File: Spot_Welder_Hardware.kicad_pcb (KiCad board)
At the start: 2 copper layers, 147 parts, among them J1 Mini USB, J2 Conn_01x03_Male, Q1 Q_NMOS_GSD, Q10 Q_NMOS_GDS, Q11 Q_NMOS_GDS, Q12 Q_NMOS_GDS, Q13 Q_NMOS_GDS, Q2 2N2219, Q3 Q_NMOS_GDS, Q4 Q_NMOS_GDS, Q5 Q_NMOS_GDS, Q6 Q_NMOS_GDS, Q7 Q_NMOS_GDS, Q8 Q_NMOS_GDS, Q9 Q_NMOS_GDS, SW1 SW_Push, SW2 SW_SPDT, SW3 Lead Voltage Trigger, SW4 SW_Push, U1 OKI, U2 ATMEGA328P, U3 FAN3122TMXCT-ND, U4 FT232RL, U5 FAN3122TMXCT-ND, Y1 Crystal

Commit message: Started board layout
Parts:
- moved D10 581.1 mm to (-103.8, 214.6)
- moved R20 560.5 mm to (-113.7, 199.4)
- moved R18 556.0 mm to (-105.2, 190.5)
- moved R23 502.9 mm to (-39.2, 41.9)
- moved R36 500.8 mm to (-39.2, 55.2)
- moved R19 500.3 mm to (-98.3, 201.3)
- moved Conn2 492.8 mm to (-68.6, 156.2)
- moved L2 481.3 mm to (-32.9, 42.5)
- moved R26 475.0 mm to (-39.2, 43.8)
- moved L7 469.8 mm to (-32.9, 52.1)
- moved R30 469.4 mm to (-39.2, 49.5)
- moved R28 466.3 mm to (-39.2, 45.7)
- moved R38 451.0 mm to (-39.2, 57.1)
- moved L4 442.6 mm to (-32.9, 46.4)
- moved Q2 438.4 mm to (-117.5, 189.2)
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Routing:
- net Net-(R13-Pad1): track 0.00 -> 7.62 mm
- net Net-(R12-Pad1): track 0.00 -> 7.62 mm
- net Net-(R25-Pad2): track 0.00 -> 3.17 mm
- net Net-(R24-Pad2): track 0.00 -> 3.17 mm
- added copper zone on F.Cu, net GND
- added copper zone on B.Cu, net V+

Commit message: High-lvel power placemet
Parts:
- D12, R21: moved to B.Cu
- moved Q3 434.1 mm to (-65.8, 23.7)
- moved SW2 426.9 mm to (-84.2, 22.9), turned to 90 degrees
- moved SW4 400.0 mm to (19.1, 139.1)
- moved D12 381.6 mm to (-40.6, 3.81)
- moved R21 365.3 mm to (-40.5, 6.99)
- moved C43 353.9 mm to (-39.1, 30.2), turned to 270 degrees
- moved U1 337.5 mm to (-41.0, 27.3), turned to 270 degrees
- moved C44 321.9 mm to (-39.1, 34.6), turned to 270 degrees
- moved R14 268.8 mm to (-58.4, 0.00), turned to 180 degrees
- moved R12 262.1 mm to (-58.4, 15.2), turned to 180 degrees
- moved C32 255.9 mm to (56.5, 59.1), turned to 90 degrees
- moved C23 240.8 mm to (60.3, 59.1), turned to 180 degrees
- moved C24 237.1 mm to (60.3, 71.8), turned to 180 degrees
- moved R13 224.6 mm to (-88.9, 7.62), turned to 0 degrees
- moved C15 214.0 mm to (92.7, 34.9), turned to 90 degrees
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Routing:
- net Net-(R23-Pad2): track 0.00 -> 185.0 mm
- net Net-(R31-Pad2): track 0.00 -> 122.6 mm
- net VIN: track 0.00 -> 22.6 mm
- net Net-(Q2-Pad3): track 0.00 -> 16.8 mm
- net VS: track 0.00 -> 10.4 mm
- net Net-(Q2-Pad2): track 0.00 -> 10.4 mm
- net Net-(L6-Pad1): track 0.00 -> 8.11 mm
- net Net-(L5-Pad1): track 0.00 -> 7.22 mm
- net GND: track 0.00 -> 6.02 mm
- net Pulse_Out: track 0.00 -> 5.71 mm
- net Net-(L9-Pad1): track 0.00 -> 4.79 mm
- net Net-(L8-Pad1): track 0.00 -> 4.79 mm
- net Net-(L10-Pad1): track 0.00 -> 4.79 mm
- net Net-(L3-Pad1): track 0.00 -> 4.71 mm
- net Net-(L2-Pad1): track 0.00 -> 4.71 mm
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- added copper zone on B.Cu, net GND
- added copper zone on F.Cu, net V+
- removed copper zone on F.Cu, net GND
- removed copper zone on B.Cu, net V+

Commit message: Placed components and routed all signal
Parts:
- Conn3: value Anderson_2 -> AndersonPP
- moved J1 611.4 mm to (-50.2, 78.9), turned to 90 degrees
- moved D17 591.9 mm to (-36.8, 81.7)
- moved R35 591.9 mm to (-36.8, 77.0)
- moved D18 591.3 mm to (-34.3, 81.7)
- moved R37 591.3 mm to (-34.3, 77.0)
- moved D20 590.7 mm to (-31.8, 81.7)
- moved R39 590.7 mm to (-31.8, 77.0)
- moved C46 589.5 mm to (-48.2, 68.5), turned to 270 degrees
- moved C47 583.3 mm to (-45.8, 68.5), turned to 90 degrees
- moved U4 580.7 mm to (-45.2, 59.7), turned to 270 degrees
- moved C48 568.5 mm to (-39.7, 53.3), turned to 0 degrees
- moved J2 552.9 mm to (-41.9, 81.3), turned to 180 degrees
- moved SW1 550.8 mm to (-76.2, 73.7), turned to 180 degrees
- moved D8 548.4 mm to (18.7, 33.0), turned to 180 degrees
- moved R10 546.2 mm to (24.0, 33.0), turned to 0 degrees
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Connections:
- C43 pad 1: VIN -> /Vin
- C45 pad 1: VIN -> /Vin
- Conn3 pad 1: V+ -> Conn_GND
- Conn3 pad 2: Conn_GND -> V+
- D12 pad 1: VIN -> /Vin
- R21 pad 1: VIN -> /Vin
- U1 pad 1: VIN -> /Vin
- U2 pad 14: 5V_Ind -> (no net)
- U2 pad 15: 7.5V_Ind -> 12.5V_Ind
- U2 pad 17: 12.5V_Ind -> 7.5V_Ind
- U2 pad 18: (no net) -> 5V_Ind
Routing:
- net Reset: track 0.00 -> 110.1 mm
- net Pulse_Out: track 5.71 -> 113.0 mm, vias 0 -> 2
- net IC_TX: track 0.00 -> 83.8 mm, vias 0 -> 1
- net IC_RX: track 0.00 -> 79.4 mm, vias 0 -> 1
- net USB+5V: track 0.00 -> 59.5 mm, vias 0 -> 2
- net Buzzer: track 0.00 -> 29.9 mm
- net Net-(D18-Pad1): track 0.00 -> 27.6 mm
- net Net-(D17-Pad1): track 0.00 -> 26.6 mm
- net DTR: track 0.00 -> 26.3 mm, vias 0 -> 1
- net 5V_Ind: track 0.00 -> 23.7 mm
- net Lead_Sense: track 0.00 -> 23.1 mm
- net V_Sense: track 0.00 -> 21.6 mm
- net Ext_Trigger: track 0.00 -> 19.1 mm
- net 7.5V_Ind: track 0.00 -> 19.0 mm
- net D-: track 0.00 -> 17.7 mm
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
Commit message: Moved around Components
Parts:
- moved R3 1.61 mm to (-7.62, 76.0)
- moved R6 1.61 mm to (-5.08, 76.0)
- moved R8 1.61 mm to (-10.2, 76.0)
- moved D2 1.27 mm to (-7.62, 81.1)
- moved D4 1.27 mm to (-5.08, 81.1)
- moved D6 1.27 mm to (-10.2, 81.1)
- moved R35 0.97 mm to (-36.8, 76.0)
- moved R37 0.97 mm to (-34.3, 76.0)
- moved R39 0.97 mm to (-31.8, 76.0)
- moved D17 0.64 mm to (-36.8, 81.1)
- moved D18 0.64 mm to (-34.3, 81.1)
- moved D20 0.64 mm to (-31.8, 81.1)
- moved R1 0.59 mm to (22.9, 76.0)
- moved R5 0.59 mm to (20.3, 76.0)
- moved R7 0.59 mm to (17.8, 76.0)
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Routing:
- net USB+5V: track 59.5 -> 51.5 mm
- net Ext_Trigger: track 19.1 -> 17.7 mm
- net 7.5V_Ind: track 19.0 -> 18.5 mm
- net 5V_Ind: track 23.7 -> 23.1 mm
- net 12.5V_Ind: track 8.96 -> 8.37 mm
- net 10V_Ind: track 14.0 -> 13.4 mm
- net Net-(D17-Pad1): track 26.6 -> 26.0 mm
- removed copper zone on B.Cu, net GND
- removed copper zone on F.Cu, net V+

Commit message: Created Polygons
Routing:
- added copper zone on F.Cu, net +5V
- added copper zone on F.Cu, net /Vin
- added copper zone on B.Cu, net GND
- added copper zone on B.Cu, net Power_GND
- added copper zone on F.Cu, net V+
- added copper zone on F.Cu, net VS
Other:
- board outline added: 256.5 x 182.9 mm
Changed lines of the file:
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@@
   (general
     (thickness 1.6)
-    (drawings 3)
+    (drawings 10)
     (tracks 349)
     (zones 0)
@@
   )
   (setup
-    (last_trace_width 0.381)
+    (last_trace_width 0.25)
     (user_trace_width 0.254)
     (user_trace_width 0.381)
@@
     )
   )
-  (gr_line (start 53.975 83.82) (end -92.075 83.82) (layer Edge.Cuts) (width 0.15))
+  (gr_line (start 160.02 83.82) (end -86.36 83.82) (layer Edge.Cuts) (width 0.15))
+  (gr_line (start 165.1 78.74) (end 165.1 -93.98) (layer Edge.Cuts) (width 0.15))
+  (gr_line (start 160.02 -99.06) (end -86.36 -99.06) (layer Edge.Cuts) (width 0.15))
+  (gr_arc (start 160.02 -93.98) (end 165.1 -93.98) (angle -90) (layer Edge.Cuts) (width 0.15))
+  (gr_arc (start 160.02 78.74) (end 160.02 83.82) (angle -90) (layer Edge.Cuts) (width 0.15))
+  (gr_arc (start -86.36 78.74) (end -91.44 78.74) (angle -90) (layer Edge.Cuts) (width 0.15))
+  (gr_arc (start -86.36 -93.98) (end -86.36 -99.06) (angle -90) (layer Edge.Cuts) (width 0.15))
+  (gr_line (start -91.44 78.74) (end -91.44 -93.98) (layer Edge.Cuts) (width 0.15))
   (gr_line (start -91.44 254) (end -91.44 -254) (layer F.SilkS) (width 0.2))
   (gr_line (start -254 84.836) (end 254 84.836) (layer F.SilkS) (width 0.2))
@@
   (segment (start -39.751 29.845) (end -39.116 29.21) (width 0.381) (layer F.Cu) (net 74))
   (segment (start -42.291 29.845) (end -39.751 29.845) (width 0.381) (layer F.Cu) (net 74))
+  (zone (net 27) (net_name VS) (layer F.Cu) (hatch edge 0.508)
+    (connect_pads yes (clearance 0.508))
+    (min_thickness 0.254)
+    (fill yes (arc_segments 16) (thermal_gap 0.508) (thermal_bridge_width 0.508))
+    (polygon
+      (pts
+        (xy 68.58 83.82) (xy 68.58 42.545) (xy 113.03 42.545) (xy 113.03 83.82)
+      )
+    )
+  )
+  (zone (net 3) (net_name V+) (layer F.Cu) (hatch edge 0.508)
+    (connect_pads (clearance 0.508))
+    (min_thickness 0.254)
+    (fill yes (arc_segments 16) (thermal_gap 0.508) (thermal_bridge_width 0.508))
+    (polygon
+      (pts
+        (xy 113.538 83.82) (xy 113.538 42.164) (xy 68.072 42.164) (xy 68.072 83.82) (xy 57.404 83.82)
+        (xy 57.404 26.416) (xy -23.876 26.416) (xy -23.876 -4.064) (xy -56.134 -4.064) (xy -56.134 69.596)
+        (xy -91.44 69.596) (xy -91.44 -99.06) (xy 165.1 -99.06) (xy 165.1 83.82)
+      )
+    )
+  )
+  (zone (net 1) (net_name +5V) (layer F.Cu) (hatch edge 0.508)
+    (connect_pads yes (clearance 0.508))
+    (min_thickness 0.254)
+    (fill yes (arc_segments 16) (thermal_gap 0.508) (thermal_bridge_width 0.508))
+    (polygon
+      (pts
+        (xy 56.896 83.82) (xy 56.896 26.924) (xy -23.876 26.924) (xy -23.876 32.766) (xy -55.626 33.02)
+        (xy -55.626 70.104) (xy -91.44 70.104) (xy -91.44 83.82) (xy 46.99 83.82)
+      )
+    )
+  )
+  (zone (net 74) (net_name /Vin) (layer F.Cu) (hatch edge 0.508)
+    (connect_pads (clearance 0.508))
+    (min_thickness 0.254)
+    (fill yes (arc_segments 16) (thermal_gap 0.508) (thermal_bridge_width 0.508))
+    (polygon
+      (pts
+        (xy -24.384 32.258) (xy -55.626 32.512) (xy -55.626 -3.556) (xy -24.384 -3.556)
+      )
+    )
+  )
+  (zone (net 4) (net_name GND) (layer B.Cu) (hatch edge 0.508)
+    (connect_pads yes (clearance 0.508))
+    (min_thickness 0.254)
+    (fill yes (arc_segments 16) (thermal_gap 0.508) (thermal_bridge_width 0.508))
+    (polygon
+      (pts
+        (xy 165.1 83.82) (xy 165.1 -99.06) (xy -91.44 -99.06) (xy -91.44 19.558) (xy -57.404 19.558)
+        (xy -57.404 69.85) (xy -91.44 69.85) (xy -91.44 83.82)
+      )
+    )
+  )
+  (zone (net 25) (net_name Power_GND) (layer B.Cu) (hatch edge 0.508)
+    (connect_pads yes (clearance 0.508))
+    (min_thickness 0.254)
+    (fill yes (arc_segments 16) (thermal_gap 0.508) (thermal_bridge_width 0.508))
+    (polygon
+      (pts
+        (xy -91.44 69.342) (xy -57.912 69.342) (xy -57.912 20.066) (xy -91.44 20.066)
+      )
+    )
+  )
 )

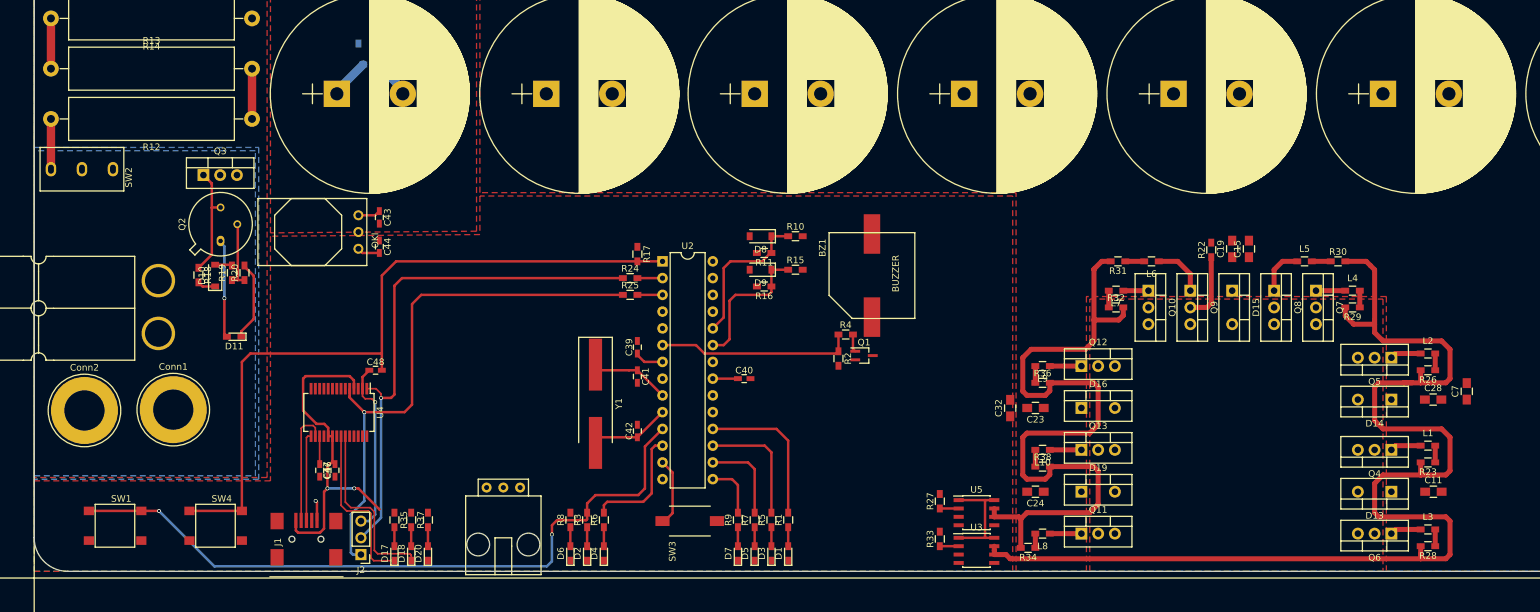
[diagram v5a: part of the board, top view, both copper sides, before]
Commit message: Finished Fill Zones and grounding
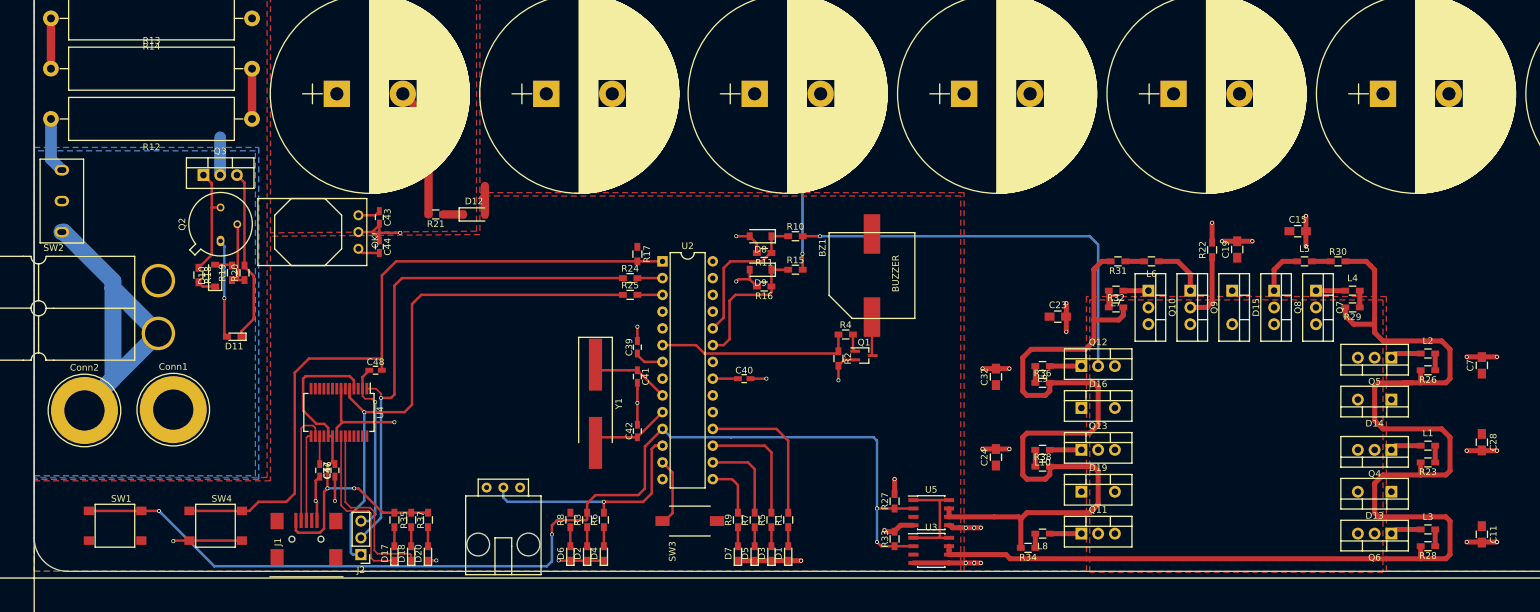
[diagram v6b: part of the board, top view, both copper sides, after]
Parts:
- D12, R21: moved to F.Cu
- moved D12 30.4 mm to (-24.8, 29.7)
- moved R21 24.8 mm to (-30.6, 29.7), turned to 180 degrees
- moved C23 14.3 mm to (63.7, 45.2), turned to 0 degrees
- moved C28 9.81 mm to (128.0, 64.2), turned to 270 degrees
- moved C11 9.78 mm to (128.0, 78.2), turned to 270 degrees
- moved C24 7.95 mm to (54.4, 66.5), turned to 90 degrees
- moved C15 7.86 mm to (100.1, 32.3), turned to 0 degrees
- moved R27 6.86 mm to (39.0, 73.2)
- moved R33 6.86 mm to (39.0, 78.9)
- moved U3 6.86 mm to (44.5, 80.6)
- moved U5 6.86 mm to (44.5, 74.9)
- moved SW2 5.71 mm to (-87.2, 27.7), turned to 0 degrees
- moved C32 5.21 mm to (54.4, 54.3)
- moved C7 4.55 mm to (128.0, 52.6)
- moved C19 0.77 mm to (90.9, 35.0)
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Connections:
- SW3 pad 1: V+ -> +5V
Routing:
- net GND: track 9.05 -> 178.6 mm, vias 1 -> 39
- net VS: track 10.4 -> 74.2 mm, vias 0 -> 1
- net Pulse_Out: track 113.1 -> 167.3 mm, vias 2 -> 4
- net Conn_GND: track 0.00 -> 52.8 mm
- net V+: track 2.80 -> 20.2 mm, vias 0 -> 2
- net Ext_Trigger: track 17.7 -> 35.0 mm, vias 0 -> 1
- net Power_GND: track 12.1 -> 26.3 mm
- net USB+5V: track 51.5 -> 59.0 mm
- net Net-(R23-Pad2): track 183.8 -> 190.7 mm
- net Net-(R31-Pad2): track 114.9 -> 121.7 mm
- net Net-(BZ1-Pad2): track 0.00 -> 5.88 mm
- net Reset: track 110.1 -> 107.2 mm
- net /Vin: track 9.54 -> 6.94 mm
- net Net-(R12-Pad2): track 7.62 -> 8.43 mm

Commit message: Added 6-32 Mounting Holes
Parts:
- added REF**: 6-32 Screw Hole, Project Library:6-32 Screw Hole, F.Cu at (-98.8, 78.0)
- added REF**: 6-32 Screw Hole, Project Library:6-32 Screw Hole, F.Cu at (-87.6, 78.7)
- added REF**: 6-32 Screw Hole, Project Library:6-32 Screw Hole, F.Cu at (162.6, -96.5)
- added REF**: 6-32 Screw Hole, Project Library:6-32 Screw Hole, F.Cu at (-88.9, -96.5)
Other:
- outline, holes or cut-outs redrawn
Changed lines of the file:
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@@
   (general
     (thickness 1.6)
-    (drawings 10)
+    (drawings 14)
     (tracks 525)
     (zones 0)
-    (modules 147)
+    (modules 151)
     (nets 75)
   )
@@
   )
   (setup
-    (last_trace_width 1.27)
+    (last_trace_width 0.25)
     (user_trace_width 0.254)
     (user_trace_width 0.381)
@@
     (mod_text_size 1 1)
     (mod_text_width 0.15)
-    (pad_size 1.524 1.524)
+    (pad_size 3.683 3.683)
     (pad_drill 0.762)
     (pad_to_mask_clearance 0.2)
@@
     (add_net V_Sense)
   )
+  (module "Project Library:6-32 Screw Hole" (layer F.Cu)
+    (at -98.806 77.978)
+    (fp_text reference REF** (at 0 0.5) (layer F.SilkS) hide
+      (effects (font (size 1 1) (thickness 0.15)))
+    )
+    (fp_text value "6-32 Screw Hole" (at 0 -0.5) (layer F.Fab)
+      (effects (font (size 1 1) (thickness 0.15)))
+    )
+    (pad "" np_thru_hole circle (at 261.366 0.762) (size 3.683 3.683) (drill 0.762) (layers *.Cu *.Mask))
+  )
+  (module "Project Library:6-32 Screw Hole" (layer F.Cu)
+    (at -87.63 78.74)
+    (fp_text reference REF** (at 0 0.5) (layer F.SilkS) hide
+      (effects (font (size 1 1) (thickness 0.15)))
+    )
+    (fp_text value "6-32 Screw Hole" (at 0 -0.5) (layer F.Fab)
+      (effects (font (size 1 1) (thickness 0.15)))
+    )
+    (pad "" np_thru_hole circle (at -1.27 0) (size 3.683 3.683) (drill 0.762) (layers *.Cu *.Mask))
+  )
+  (module "Project Library:6-32 Screw Hole" (layer F.Cu)
+    (at 162.56 -96.52)
+    (fp_text reference REF** (at 0 0.5) (layer F.SilkS) hide
+      (effects (font (size 1 1) (thickness 0.15)))
+    )
+    (fp_text value "6-32 Screw Hole" (at 0 -0.5) (layer F.Fab)
+      (effects (font (size 1 1) (thickness 0.15)))
+    )
+    (pad "" np_thru_hole circle (at 0 0) (size 3.683 3.683) (drill 0.762) (layers *.Cu *.Mask))
+  )
   (module MRDT_Devices:BUZZER_SMI_1324_TW_5V_2_R (layer F.Cu)
     (at 35.56 32.48 270)
@@
     )
   )
+  (module "Project Library:6-32 Screw Hole" (layer F.Cu)
+    (at -88.9 -96.52)
+    (fp_text reference REF** (at 0 0.5) (layer F.SilkS) hide
+      (effects (font (size 1 1) (thickness 0.15)))
+    )
+    (fp_text value "6-32 Screw Hole" (at 0 -0.5) (layer F.Fab)
+      (effects (font (size 1 1) (thickness 0.15)))
+    )
+    (pad "" np_thru_hole circle (at 0 0) (size 3.683 3.683) (drill 0.762) (layers *.Cu *.Mask))
+  )
+  (gr_line (start -91.44 -98.044) (end -91.44 -93.98) (layer Edge.Cuts) (width 0.15))
+  (gr_line (start -86.36 -99.06) (end -90.424 -99.06) (layer Edge.Cuts) (width 0.15))
+  (gr_arc (start -90.424 -98.044) (end -90.424 -99.06) (angle -90) (layer Edge.Cuts) (width 0.15))
+  (gr_line (start 164.084 -99.06) (end 160.02 -99.06) (layer Edge.Cuts) (width 0.15))
+  (gr_line (start 165.1 -93.98) (end 165.1 -98.044) (layer Edge.Cuts) (width 0.15))
+  (gr_arc (start 164.084 -98.044) (end 165.1 -98.044) (angle -90) (layer Edge.Cuts) (width 0.15))
   (gr_line (start 160.02 83.82) (end -86.36 83.82) (layer Edge.Cuts) (width 0.15))
   (gr_line (start 165.1 78.74) (end 165.1 -93.98) (layer Edge.Cuts) (width 0.15))
   (gr_line (start 160.02 -99.06) (end -86.36 -99.06) (layer Edge.Cuts) (width 0.15))
-  (gr_arc (start 160.02 -93.98) (end 165.1 -93.98) (angle -90) (layer Edge.Cuts) (width 0.15))
   (gr_arc (start 160.02 78.74) (end 160.02 83.82) (angle -90) (layer Edge.Cuts) (width 0.15))
   (gr_arc (start -86.36 78.74) (end -91.44 78.74) (angle -90) (layer Edge.Cuts) (width 0.15))
-  (gr_arc (start -86.36 -93.98) (end -86.36 -99.06) (angle -90) (layer Edge.Cuts) (width 0.15))
   (gr_line (start -91.44 78.74) (end -91.44 -93.98) (layer Edge.Cuts) (width 0.15))
   (gr_line (start -91.44 254) (end -91.44 -254) (layer F.SilkS) (width 0.2))
@@
   (segment (start -65.913 40.64) (end -66.548 40.005) (width 0.381) (layer F.Cu) (net 3))
   (segment (start -64.008 40.64) (end -65.913 40.64) (width 0.381) (layer F.Cu) (net 3))
+  (via (at 25.019 35.687) (size 0.6) (drill 0.4) (layers F.Cu B.Cu) (net 3))
+  (segment (start 25.06 38.1) (end 25.06 35.728) (width 0.381) (layer F.Cu) (net 3))
+  (segment (start 25.06 35.728) (end 25.019 35.687) (width 0.381) (layer F.Cu) (net 3))
+  (via (at 25.019 25.019) (size 0.6) (drill 0.4) (layers F.Cu B.Cu) (net 3))
+  (segment (start 25.019 35.687) (end 25.019 25.019) (width 0.381) (layer B.Cu) (net 3))
+  (segment (start -23.116 29.718) (end -23.116 25.402) (width 1.27) (layer F.Cu) (net 3))
   (via (at 125.73 79.375) (size 0.6) (drill 0.4) (layers F.Cu B.Cu) (net 4))
   (segment (start 128.016 79.375) (end 125.73 79.375) (width 0.762) (layer F.Cu) (net 4))
@@
   (via (at 125.73 65.532) (size 0.6) (drill 0.4) (layers F.Cu B.Cu) (net 4))
   (segment (start 128.016 65.532) (end 125.73 65.532) (width 0.762) (layer F.Cu) (net 4))
-  (via (at 25.019 35.687) (size 0.6) (drill 0.4) (layers F.Cu B.Cu) (net 3))
-  (segment (start 25.06 38.1) (end 25.06 35.728) (width 0.381) (layer F.Cu) (net 3))
-  (segment (start 25.06 35.728) (end 25.019 35.687) (width 0.381) (layer F.Cu) (net 3))
-  (via (at 25.019 25.019) (size 0.6) (drill 0.4) (layers F.Cu B.Cu) (net 3))
-  (segment (start 25.019 35.687) (end 25.019 25.019) (width 0.381) (layer B.Cu) (net 3))
-  (segment (start -23.116 29.718) (end -23.116 25.402) (width 1.27) (layer F.Cu) (net 3))
   (via (at 125.73 51.308) (size 0.6) (drill 0.4) (layers F.Cu B.Cu) (net 4))
   (segment (start 128.016 51.308) (end 125.73 51.308) (width 0.762) (layer F.Cu) (net 4))
